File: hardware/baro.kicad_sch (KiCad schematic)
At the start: 2 parts, among them U30 BMP388

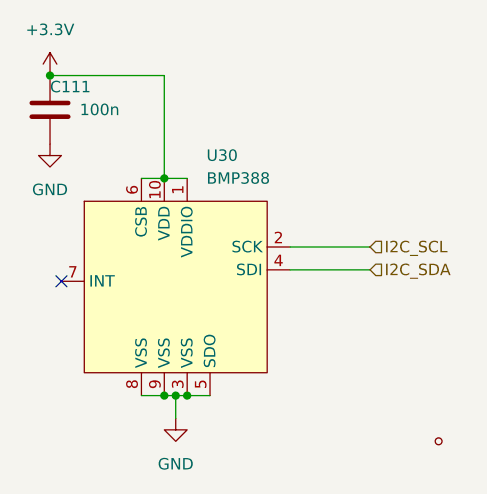
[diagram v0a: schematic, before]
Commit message: switched to 0201
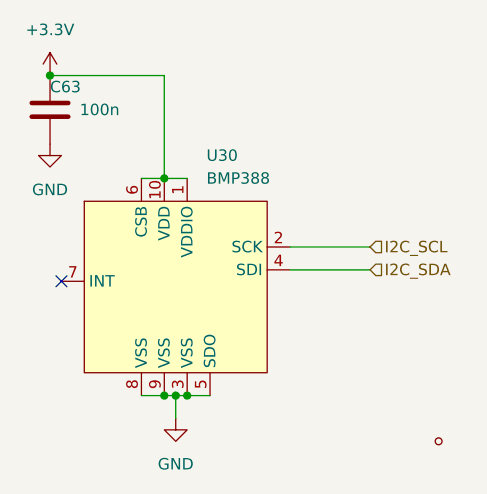
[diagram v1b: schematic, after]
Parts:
- removed C111: 100n, Capacitor_SMD:C_0402_1005Metric, symbol Device:C
- added C63: 100n, Capacitor_SMD:C_0201_0603Metric, symbol Device:C
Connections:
- net +3.3V: now also C63.1
- net GND: now also C63.2
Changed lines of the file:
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@@
 	(paper "A5")
 	(junction
+		(at 100.33 55.88)
+		(diameter 0)
+		(color 0 0 0 0)
+	)
+	(junction
+		(at 102.87 80.01)
+		(diameter 0)
+		(color 0 0 0 0)
+	)
+	(junction
+		(at 101.6 80.01)
+		(diameter 0)
+		(color 0 0 0 0)
+	)
+	(junction
 		(at 87.63 44.45)
-		(diameter 0)
-		(color 0 0 0 0)
-	)
-	(junction
-		(at 100.33 55.88)
-		(diameter 0)
-		(color 0 0 0 0)
-	)
-	(junction
-		(at 102.87 80.01)
-		(diameter 0)
-		(color 0 0 0 0)
-	)
-	(junction
-		(at 101.6 80.01)
 		(diameter 0)
 		(color 0 0 0 0)
@@
 	)
 	(symbol
-		(lib_id "Device:C")
-		(at 87.63 48.26 0)
-		(unit 1)
-		(exclude_from_sim no)
-		(in_bom yes)
-		(on_board yes)
-		(dnp no)
-		(property "Reference" "C111"
-			(at 87.63 45.72 0)
-			(effects
-				(font
-					(size 1.27 1.27)
-				)
-				(justify left)
-			)
-		)
-		(property "Value" "100n"
-			(at 90.932 48.26 0)
-			(effects
-				(font
-					(size 1.27 1.27)
-				)
-				(justify left)
-			)
-		)
-		(property "Footprint" "Capacitor_SMD:C_0402_1005Metric"
-			(at 88.5952 52.07 0)
-			(effects
-				(font
-					(size 1.27 1.27)
-				)
-				(hide yes)
-			)
-		)
-		(property "Datasheet" "~"
-			(at 87.63 48.26 0)
-			(effects
-				(font
-					(size 1.27 1.27)
-				)
-				(hide yes)
-			)
-		)
-		(property "Description" ""
-			(at 87.63 48.26 0)
-			(effects
-				(font
-					(size 1.27 1.27)
-				)
-			)
-		)
-		(property "LCSC" "C1525"
-			(at 87.63 48.26 0)
-			(effects
-				(font
-					(size 1.27 1.27)
-				)
-				(hide yes)
-			)
-		)
-		(pin "1"
-		)
-		(pin "2"
-		)
-		(instances
-			(project "OpenFC"
-				(path "/fb88b6f9-ee39-4640-a9d4-04a17ceeac64/a075ed74-3bcc-47df-aa10-c56f48bd2f3e"
-					(reference "C111")
-					(unit 1)
-				)
-			)
-		)
-	)
-	(symbol
 		(lib_id "power:+3.3V")
 		(at 87.63 44.45 0)
@@
 					(unit 1)
 				)
+			)
+		)
+	)
+	(symbol
+		(lib_id "Device:C")
+		(at 87.63 48.26 0)
+		(unit 1)
+		(exclude_from_sim no)
+		(in_bom yes)
+		(on_board yes)
+		(dnp no)
+		(property "Reference" "C63"
+			(at 87.63 45.72 0)
+			(effects
+				(font
+					(size 1.27 1.27)
+				)
+				(justify left)
+			)
+		)
+		(property "Value" "100n"
+			(at 90.932 48.26 0)
+			(effects
+				(font
+					(size 1.27 1.27)
+				)
+				(justify left)
+			)
+		)
+		(property "Footprint" "Capacitor_SMD:C_0201_0603Metric"
+			(at 88.5952 52.07 0)
+			(effects
+				(font
+					(size 1.27 1.27)
+				)
+				(hide yes)
+			)
+		)
+		(property "Datasheet" "~"
+			(at 87.63 48.26 0)
+			(effects
+				(font
+					(size 1.27 1.27)
+				)
+				(hide yes)
+			)
+		)
+		(property "Description" ""
+			(at 87.63 48.26 0)
+			(effects
+				(font
+					(size 1.27 1.27)
+				)
+			)
+		)
+		(property "LCSC" "C76939"
+			(at 87.63 48.26 0)
+			(effects
+				(font
+					(size 1.27 1.27)
+				)
+				(hide yes)
+			)
+		)
+		(pin "1"
+		)
+		(pin "2"
+		)
+		(instances
+			(project "OpenFC"
+				(path "/fb88b6f9-ee39-4640-a9d4-04a17ceeac64/a075ed74-3bcc-47df-aa10-c56f48bd2f3e"
+					(reference "C63")
+					(unit 1)
+				)
